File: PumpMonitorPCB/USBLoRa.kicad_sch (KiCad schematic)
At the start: 4 parts, among them J3 USB_C_Receptacle_USB2.0_16P, U5 TPD3E001DRLR

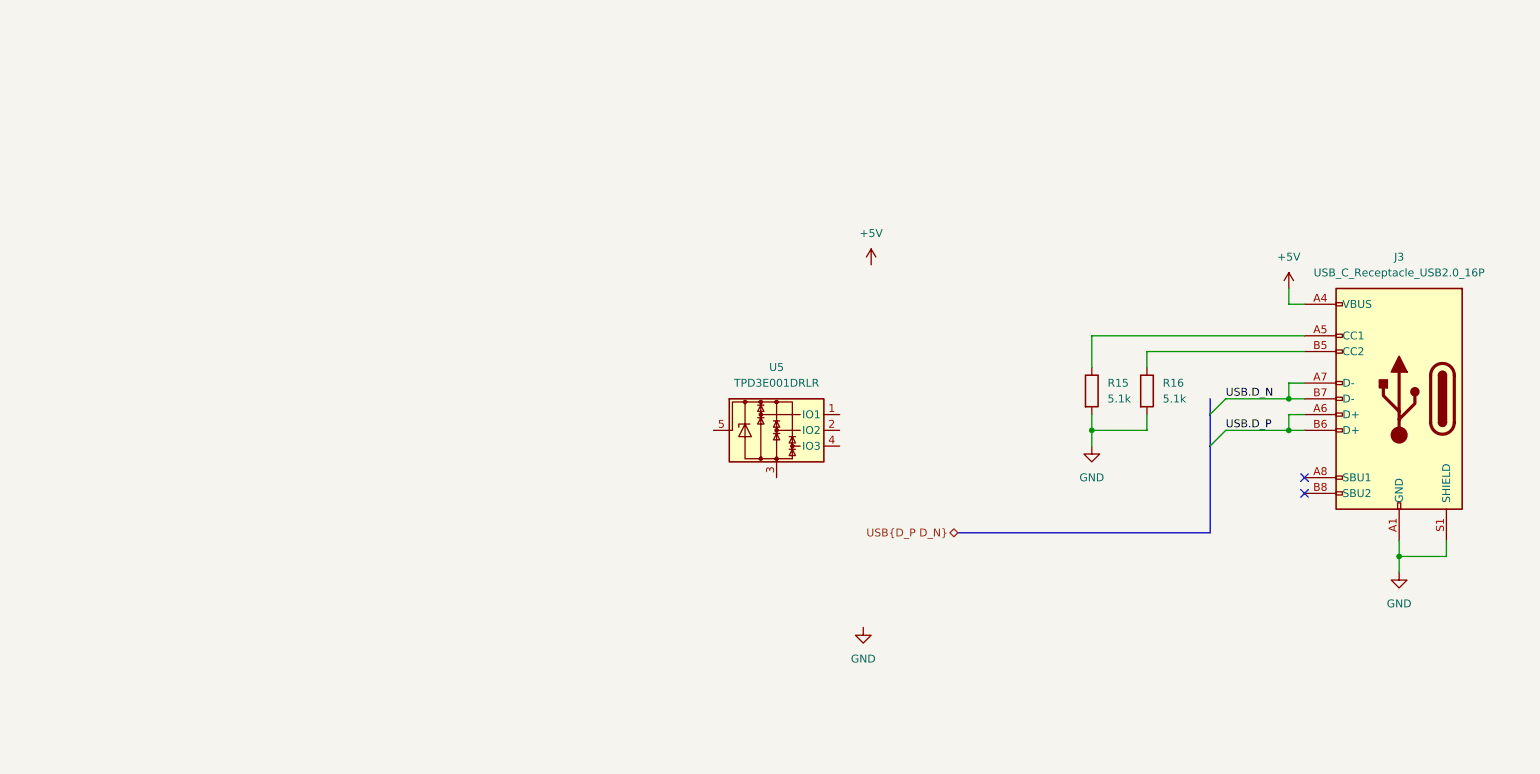
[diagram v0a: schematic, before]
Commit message: Tidied schematic, added LoRa module.
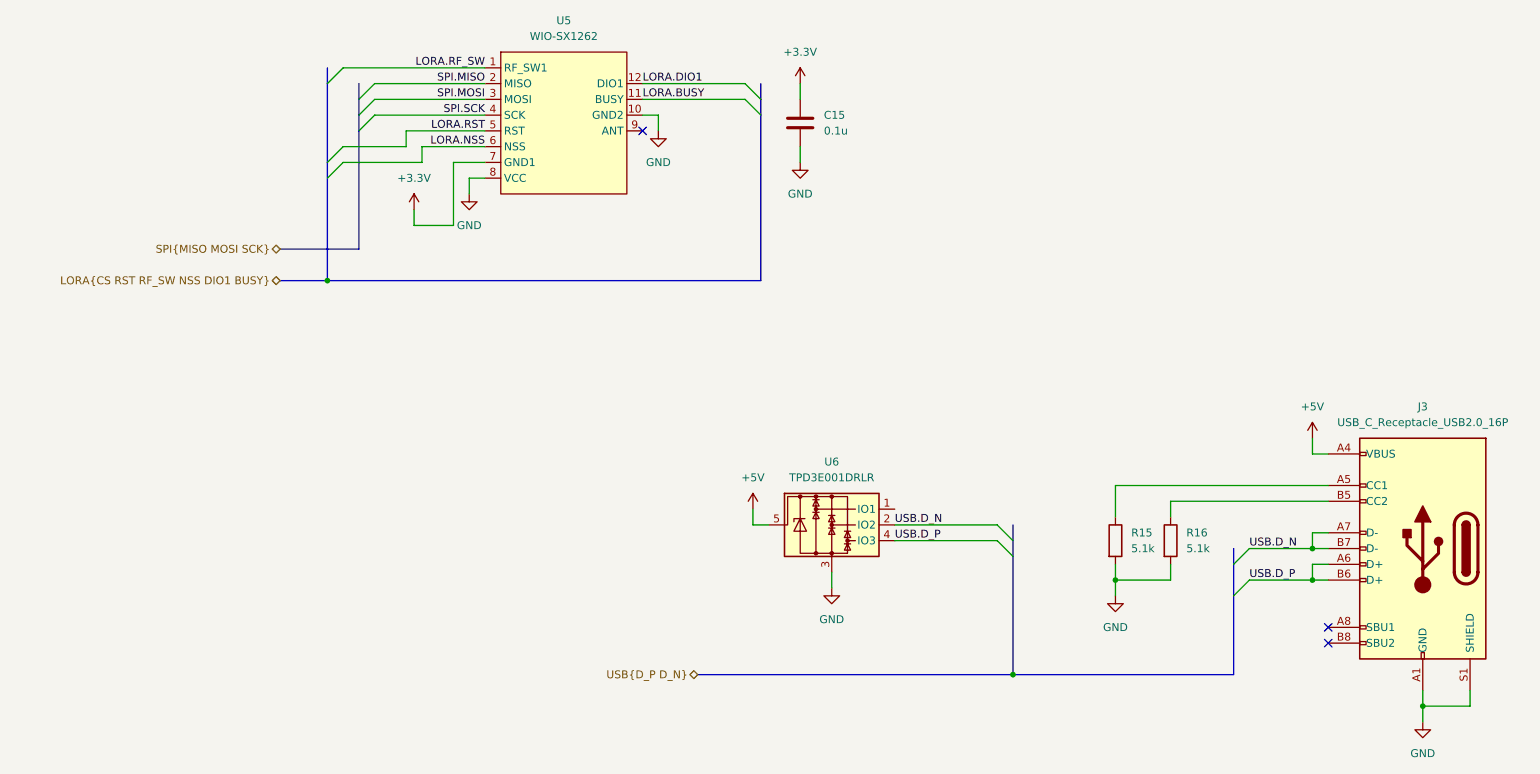
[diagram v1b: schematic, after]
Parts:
- added C15: 0.1u, symbol Device:C
- added U5: WIO-SX1262, Wio-SX1262 Module Kicad Library:Wio-SX1262 PCB Package, symbol Wio-SX1262 Schematic Package:MODULE-WIO-SX1262
- renumbered U5 to U6
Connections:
- net +5V: now also U6.5
- net GND: now also U6.3, C15.2, U5.10 (GND2), U5.8 (VCC)
- net USB.D_N: now also U6.2 (IO2)
- net USB.D_P: now also U6.4 (IO3)
- new net +3.3V: C15.1, U5.7 (GND1)
- new net LORA.BUSY: U5.11 (BUSY)
- new net LORA.DIO1: U5.12 (DIO1)
- new net LORA.NSS: U5.6 (NSS)
- new net LORA.RF_SW: U5.1 (RF_SW1)
- new net LORA.RST: U5.5 (RST)
- new net SPI.MISO: U5.2 (MISO)
- new net SPI.MOSI: U5.3 (MOSI)
- new net SPI.SCK: U5.4 (SCK)
- no-connect marks 2 -> 3
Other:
- title: Pump monitor - USB -> Pump monitor - USB and LoRa transceiver
- moved on the sheet: J3, R15, R16, U6

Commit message: Added aux. connectors, started assigning components.
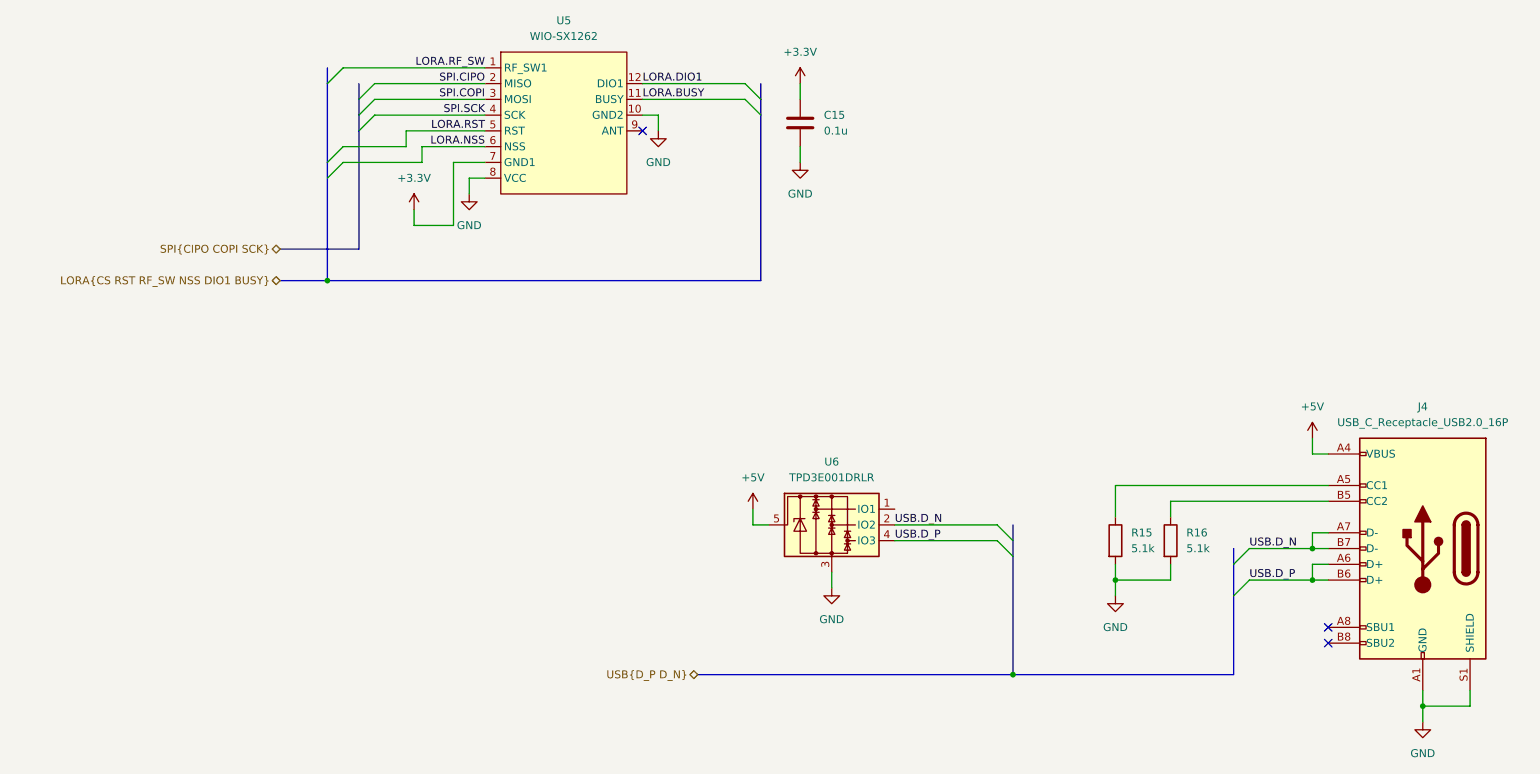
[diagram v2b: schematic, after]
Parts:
- C15: footprint (none) -> Capacitor_SMD:C_0805_2012Metric_Pad1.18x1.45mm_HandSolder
- R15, R16: footprint Resistor_SMD:R_0603_1608Metric_Pad0.98x0.95mm_HandSolder -> Resistor_SMD:R_0805_2012Metric_Pad1.20x1.40mm_HandSolder
- renumbered J3 to J4
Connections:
- net SPI.MISO renamed SPI.CIPO
- net SPI.MOSI renamed SPI.COPI
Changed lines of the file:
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@@
 		)
 	)
-	(label "SPI.MOSI"
+	(label "SPI.COPI"
 		(at 92.71 44.45 180)
 		(effects
@@
 		)
 	)
-	(label "SPI.MISO"
+	(label "SPI.CIPO"
 		(at 92.71 41.91 180)
 		(effects
@@
 		)
 	)
-	(hierarchical_label "SPI{MISO MOSI SCK}"
+	(hierarchical_label "SPI{CIPO COPI SCK}"
 		(shape bidirectional)
 		(at 59.69 68.58 180)
@@
 			)
 		)
-		(property "Footprint" ""
+		(property "Footprint" "Capacitor_SMD:C_0805_2012Metric_Pad1.18x1.45mm_HandSolder"
 			(at 144.4752 52.07 0)
 			(effects
@@
 			)
 		)
-		(property "Footprint" "Resistor_SMD:R_0603_1608Metric_Pad0.98x0.95mm_HandSolder"
+		(property "Footprint" "Resistor_SMD:R_0805_2012Metric_Pad1.20x1.40mm_HandSolder"
 			(at 201.422 115.57 90)
 			(effects
@@
 			)
 		)
-		(property "Footprint" "Resistor_SMD:R_0603_1608Metric_Pad0.98x0.95mm_HandSolder"
+		(property "Footprint" "Resistor_SMD:R_0805_2012Metric_Pad1.20x1.40mm_HandSolder"
 			(at 192.532 115.57 90)
 			(effects
@@
 		(on_board yes)
 		(dnp no)
-		(property "Reference" "J3"
+		(property "Reference" "J4"
 			(at 243.84 93.98 0)
 			(effects
@@
 			(project "PumpMonitorPCB"
 				(path "/c90c4964-ca1b-44d9-8ea9-8989903af0f2/519408a1-89cc-4bd2-9b7b-cb03d2ff4d33/da0c16f9-ee3c-407f-b19e-ac24af140ef1"
-					(reference "J3")
-					(unit 1)
-				)
+					(reference "J4")
+					(unit 1)
+				)

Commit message: Added op amps to voltage and current measurement, more footprint assignments.
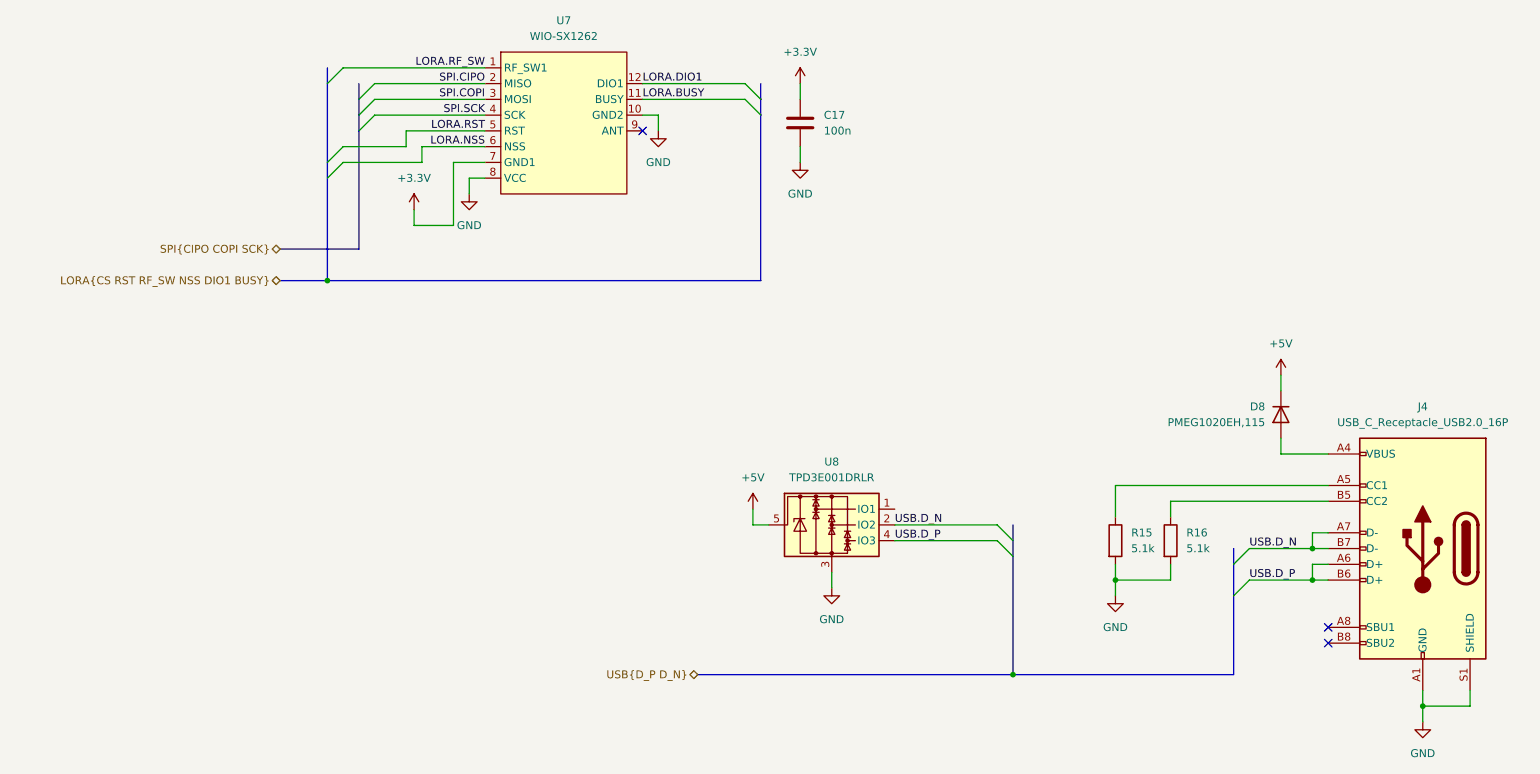
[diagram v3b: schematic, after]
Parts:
- added D8: PMEG1020EH,115, Diode_SMD:D_SOD-123F, symbol Diode:1N4004
- C17: renamed from C15; value 0.1u -> 100n
- renumbered U5 to U7, U6 to U8
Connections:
- net +5V: now also D8.1 (K); no longer J4.A4 (VBUS), J4.A9 (VBUS), J4.B4 (VBUS), J4.B9 (VBUS)
- new net: D8.2 (A), J4.A4 (VBUS), J4.A9 (VBUS), J4.B4 (VBUS), J4.B9 (VBUS)
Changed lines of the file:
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@@
 		(rev "V0.0.0")
 		(company "Jotham Gates")
+		(comment 4 "Warning: Parts of this circuit operate at mains potential.")
 	)
 	(junction
@@
 	(wire
 		(pts
+			(xy 220.98 99.06) (xy 220.98 101.6)
+		)
+		(stroke
+			(width 0)
+			(type default)
+		)
+	)
+	(wire
+		(pts
 			(xy 69.85 52.07) (xy 80.01 52.07)
 		)
@@
 	(wire
 		(pts
-			(xy 226.06 101.6) (xy 226.06 99.06)
+			(xy 220.98 91.44) (xy 220.98 88.9)
 		)
 		(stroke
@@
 		)
 	)
-	(wire
-		(pts
-			(xy 228.6 101.6) (xy 226.06 101.6)
-		)
-		(stroke
-			(width 0)
-			(type default)
-		)
-	)
 	(bus
 		(pts
@@
 		(pts
 			(xy 59.69 68.58) (xy 72.39 68.58)
+		)
+		(stroke
+			(width 0)
+			(type default)
+		)
+	)
+	(wire
+		(pts
+			(xy 220.98 101.6) (xy 228.6 101.6)
 		)
 		(stroke
@@
 		(dnp no)
 		(fields_autoplaced yes)
-		(property "Reference" "#PWR052"
+		(property "Reference" "#PWR060"
 			(at 148.59 129.54 0)
 			(effects
@@
 			(project "PumpMonitorPCB"
 				(path "/c90c4964-ca1b-44d9-8ea9-8989903af0f2/519408a1-89cc-4bd2-9b7b-cb03d2ff4d33/da0c16f9-ee3c-407f-b19e-ac24af140ef1"
-					(reference "#PWR052")
+					(reference "#PWR060")
 					(unit 1)
 				)
@@
 		(on_board yes)
 		(dnp no)
-		(property "Reference" "U6"
+		(property "Reference" "U8"
 			(at 148.59 102.87 0)
 			(effects
@@
 			(project "PumpMonitorPCB"
 				(path "/c90c4964-ca1b-44d9-8ea9-8989903af0f2/519408a1-89cc-4bd2-9b7b-cb03d2ff4d33/da0c16f9-ee3c-407f-b19e-ac24af140ef1"
-					(reference "U6")
+					(reference "U8")
 					(unit 1)
 				)
@@
 		(dnp no)
 		(fields_autoplaced yes)
-		(property "Reference" "C15"
+		(property "Reference" "C17"
 			(at 147.32 46.9899 0)
 			(effects
@@
 			)
 		)
-		(property "Value" "0.1u"
+		(property "Value" "100n"
 			(at 147.32 49.5299 0)
 			(effects
@@
 			(project "PumpMonitorPCB"
 				(path "/c90c4964-ca1b-44d9-8ea9-8989903af0f2/519408a1-89cc-4bd2-9b7b-cb03d2ff4d33/da0c16f9-ee3c-407f-b19e-ac24af140ef1"
-					(reference "C15")
+					(reference "C17")
 					(unit 1)
 				)
@@
 		(dnp no)
 		(fields_autoplaced yes)
-		(property "Reference" "#PWR051"
+		(property "Reference" "#PWR059"
 			(at 143.51 60.96 0)
 			(effects
@@
 			(project "PumpMonitorPCB"
 				(path "/c90c4964-ca1b-44d9-8ea9-8989903af0f2/519408a1-89cc-4bd2-9b7b-cb03d2ff4d33/da0c16f9-ee3c-407f-b19e-ac24af140ef1"
-					(reference "#PWR051")
+					(reference "#PWR059")
 					(unit 1)
 				)
@@
 		(dnp no)
 		(fields_autoplaced yes)
-		(property "Reference" "#PWR048"
+		(property "Reference" "#PWR056"
 			(at 120.65 55.88 0)
 			(effects
@@
 			(project "PumpMonitorPCB"
 				(path "/c90c4964-ca1b-44d9-8ea9-8989903af0f2/519408a1-89cc-4bd2-9b7b-cb03d2ff4d33/da0c16f9-ee3c-407f-b19e-ac24af140ef1"
-					(reference "#PWR048")
+					(reference "#PWR056")
 					(unit 1)
 				)
@@
 		(dnp no)
 		(fields_autoplaced yes)
-		(property "Reference" "#PWR049"
+		(property "Reference" "#PWR057"
 			(at 135.89 114.3 0)
 			(effects
@@
 			(project "PumpMonitorPCB"
 				(path "/c90c4964-ca1b-44d9-8ea9-8989903af0f2/519408a1-89cc-4bd2-9b7b-cb03d2ff4d33/da0c16f9-ee3c-407f-b19e-ac24af140ef1"
-					(reference "#PWR049")
+					(reference "#PWR057")
 					(unit 1)
 				)
@@
 		(dnp no)
 		(fields_autoplaced yes)
-		(property "Reference" "#PWR046"
+		(property "Reference" "#PWR054"
 			(at 81.28 66.04 0)
 			(effects
@@
 			(project "PumpMonitorPCB"
 				(path "/c90c4964-ca1b-44d9-8ea9-8989903af0f2/519408a1-89cc-4bd2-9b7b-cb03d2ff4d33/da0c16f9-ee3c-407f-b19e-ac24af140ef1"
-					(reference "#PWR046")
+					(reference "#PWR054")
 					(unit 1)
 				)
@@
 		(dnp no)
 		(fields_autoplaced yes)
-		(property "Reference" "U5"
+		(property "Reference" "U7"
 			(at 105.41 31.75 0)
 			(effects
@@
 			(project "PumpMonitorPCB"
 				(path "/c90c4964-ca1b-44d9-8ea9-8989903af0f2/519408a1-89cc-4bd2-9b7b-cb03d2ff4d33/da0c16f9-ee3c-407f-b19e-ac24af140ef1"
-					(reference "U5")
+					(reference "U7")
 					(unit 1)
 				)
@@
 	(symbol
 		(lib_id "power:+5V")
-		(at 226.06 99.06 0)
+		(at 220.98 88.9 0)
 		(unit 1)
 		(exclude_from_sim no)
@@
 		(dnp no)
 		(fields_autoplaced yes)
-		(property "Reference" "#PWR054"
-			(at 226.06 102.87 0)
+		(property "Reference" "#PWR062"
+			(at 220.98 92.71 0)
 			(effects
 				(font
@@
 		)
 		(property "Value" "+5V"
-			(at 226.06 93.98 0)
+			(at 220.98 83.82 0)
 			(effects
 				(font
@@
 		)
 		(property "Footprint" ""
-			(at 226.06 99.06 0)
+			(at 220.98 88.9 0)
 			(effects
 				(font
@@
 		)
 		(property "Datasheet" ""
-			(at 226.06 99.06 0)
+			(at 220.98 88.9 0)
 			(effects
 				(font
@@
 		)
 		(property "Description" "Power symbol creates a global label with name \"+5V\""
-			(at 226.06 99.06 0)
+			(at 220.98 88.9 0)
 			(effects
 				(font
@@
 			(project "PumpMonitorPCB"
 				(path "/c90c4964-ca1b-44d9-8ea9-8989903af0f2/519408a1-89cc-4bd2-9b7b-cb03d2ff4d33/da0c16f9-ee3c-407f-b19e-ac24af140ef1"
-					(reference "#PWR054")
+					(reference "#PWR062")
 					(unit 1)
 				)
@@
 		(dnp no)
 		(fields_autoplaced yes)
-		(property "Reference" "#PWR047"
+		(property "Reference" "#PWR055"
 			(at 90.17 66.04 0)
 			(effects
@@
 			(project "PumpMonitorPCB"
 				(path "/c90c4964-ca1b-44d9-8ea9-8989903af0f2/519408a1-89cc-4bd2-9b7b-cb03d2ff4d33/da0c16f9-ee3c-407f-b19e-ac24af140ef1"
-					(reference "#PWR047")
+					(reference "#PWR055")
 					(unit 1)
 				)
@@
 		(dnp no)
 		(fields_autoplaced yes)
-		(property "Reference" "#PWR053"
+		(property "Reference" "#PWR061"
 			(at 194.31 130.81 0)
 			(effects
@@
 			(project "PumpMonitorPCB"
 				(path "/c90c4964-ca1b-44d9-8ea9-8989903af0f2/519408a1-89cc-4bd2-9b7b-cb03d2ff4d33/da0c16f9-ee3c-407f-b19e-ac24af140ef1"
-					(reference "#PWR053")
+					(reference "#PWR061")
 					(unit 1)
 				)
@@
 		(dnp no)
 		(fields_autoplaced yes)
-		(property "Reference" "#PWR050"
+		(property "Reference" "#PWR058"
 			(at 143.51 45.72 0)
 			(effects
@@
 			(project "PumpMonitorPCB"
 				(path "/c90c4964-ca1b-44d9-8ea9-8989903af0f2/519408a1-89cc-4bd2-9b7b-cb03d2ff4d33/da0c16f9-ee3c-407f-b19e-ac24af140ef1"
-					(reference "#PWR050")
+					(reference "#PWR058")
 					(unit 1)
 				)
@@
 		(dnp no)
 		(fields_autoplaced yes)
-		(property "Reference" "#PWR055"
+		(property "Reference" "#PWR063"
 			(at 243.84 151.13 0)
 			(effects
@@
 			(project "PumpMonitorPCB"
 				(path "/c90c4964-ca1b-44d9-8ea9-8989903af0f2/519408a1-89cc-4bd2-9b7b-cb03d2ff4d33/da0c16f9-ee3c-407f-b19e-ac24af140ef1"
-					(reference "#PWR055")
+					(reference "#PWR063")
 					(unit 1)
 				)
+			)
+		)
+	)
+	(symbol
+		(lib_id "Diode:1N4004")
+		(at 220.98 95.25 90)
+		(mirror x)
+		(unit 1)
+		(exclude_from_sim no)
+		(in_bom yes)
+		(on_board yes)
+		(dnp no)
+		(property "Reference" "D8"
+			(at 218.44 93.9799 90)
+			(effects
+				(font
+					(size 1.27 1.27)
+				)
+				(justify left)
+			)
+		)
+		(property "Value" "PMEG1020EH,115"
+			(at 218.44 96.5199 90)
+			(effects
+				(font
+					(size 1.27 1.27)
+				)
+				(justify left)
+			)
+		)
+		(property "Footprint" "Diode_SMD:D_SOD-123F"
+			(at 225.425 95.25 0)
+			(effects
+				(font
+					(size 1.27 1.27)
+				)
+				(hide yes)
+			)
+		)
+		(property "Datasheet" "http://www.vishay.com/docs/88503/1n4001.pdf"
+			(at 220.98 95.25 0)
+			(effects
+				(font
+					(size 1.27 1.27)
+				)
+				(hide yes)
+			)
+		)
+		(property "Description" "400V 1A General Purpose Rectifier Diode, DO-41"
+			(at 220.98 95.25 0)
+			(effects
+				(font
+					(size 1.27 1.27)
+				)
+				(hide yes)
+			)
+		)
+		(property "Sim.Device" "D"
+			(at 220.98 95.25 0)
+			(effects
+				(font
+					(size 1.27 1.27)
+				)
+				(hide yes)
+			)
+		)
+		(property "Sim.Pins" "1=K 2=A"
+			(at 220.98 95.25 0)
+			(effects
+				(font
+					(size 1.27 1.27)
+				)
+				(hide yes)
+			)
+		)
+		(pin "2"
+		)
+		(pin "1"
+		)
+		(instances
+			(project "PumpMonitorPCB"
+				(path "/c90c4964-ca1b-44d9-8ea9-8989903af0f2/519408a1-89cc-4bd2-9b7b-cb03d2ff4d33/da0c16f9-ee3c-407f-b19e-ac24af140ef1"
+					(reference "D8")
+					(unit 1)
+				)
